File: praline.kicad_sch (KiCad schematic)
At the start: 0 parts

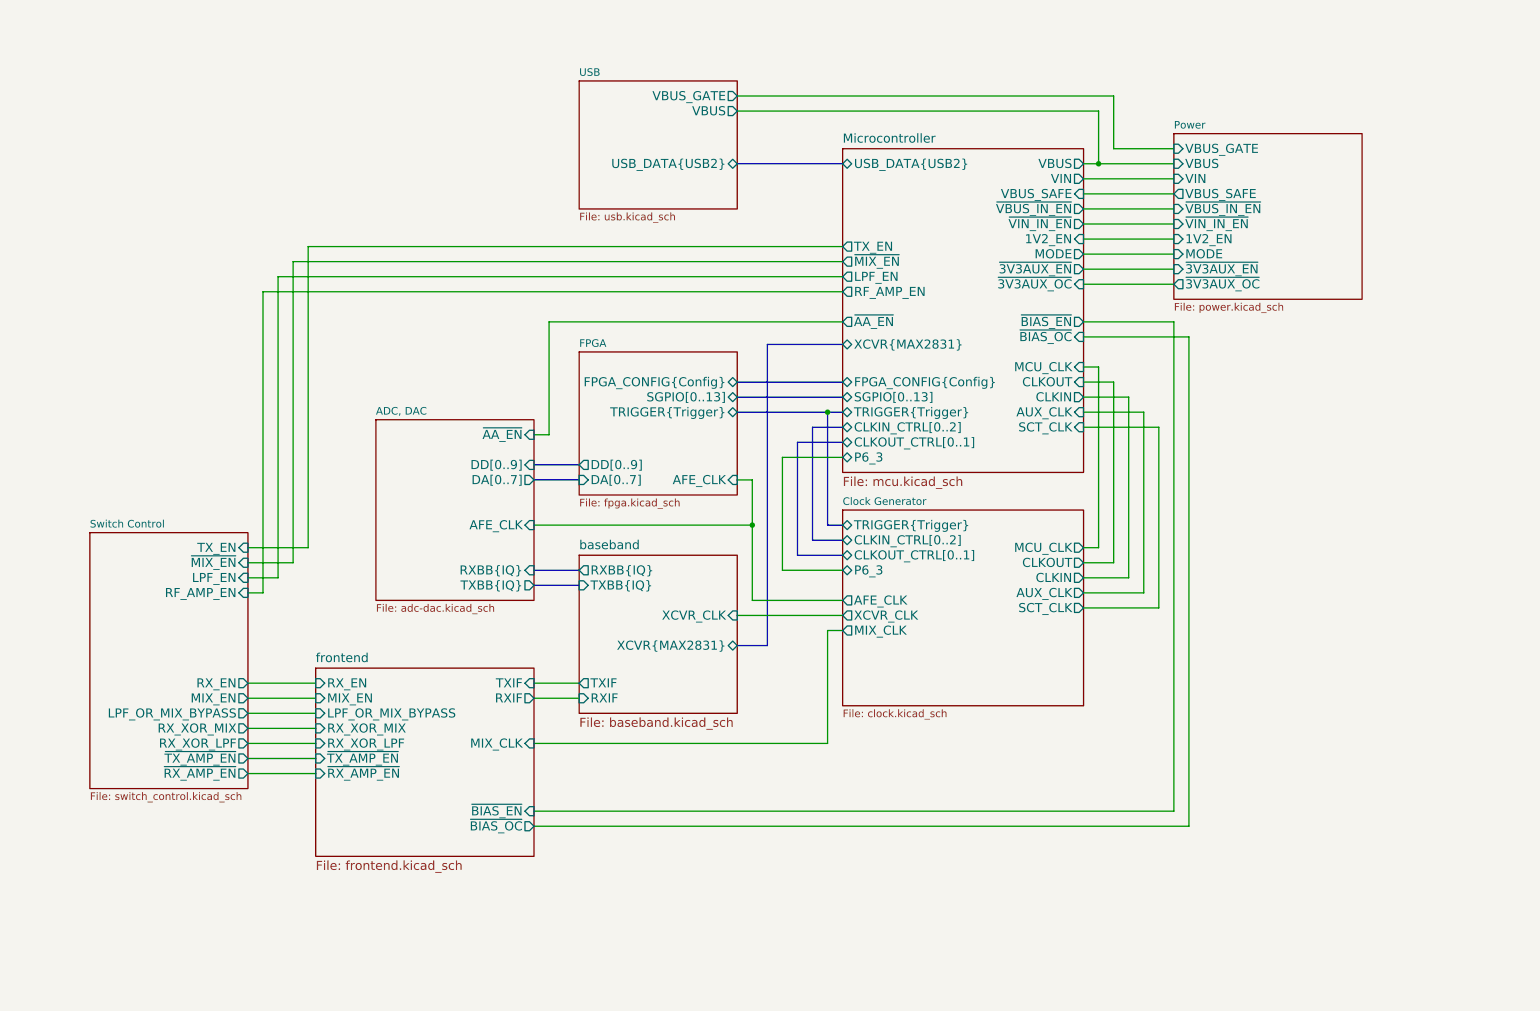
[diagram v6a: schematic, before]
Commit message: Connect mixer U4 LD and ENBL pins to MCU
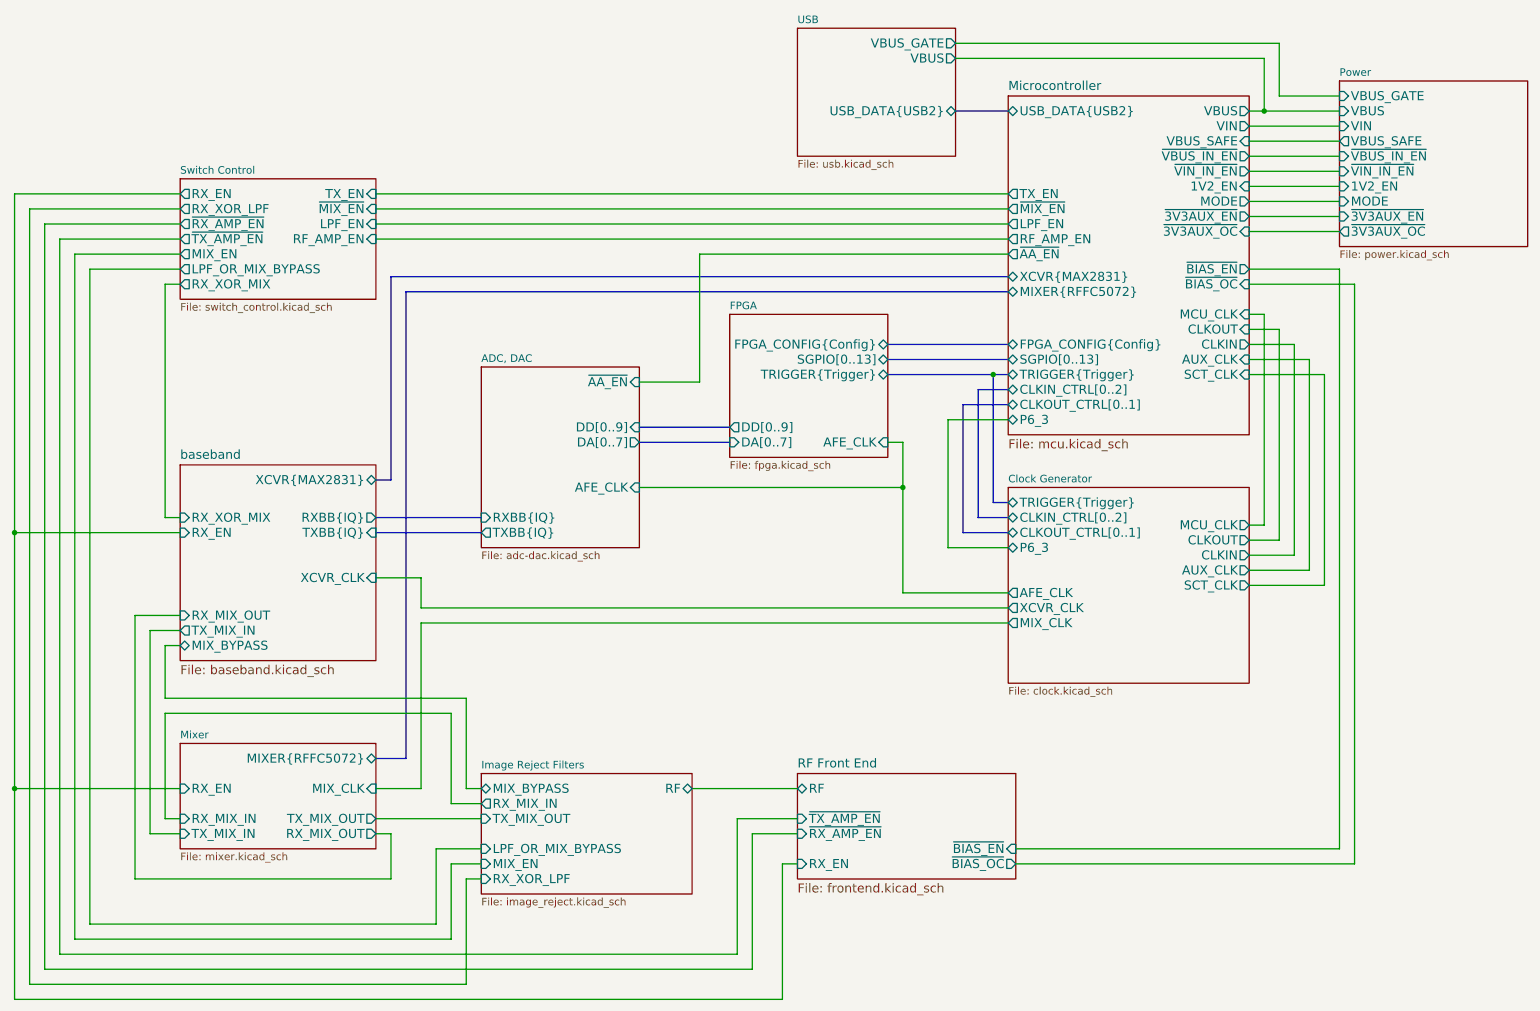
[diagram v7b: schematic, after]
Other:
- sheet frontend renamed RF Front End
- added sheet Image Reject Filters (image_reject.kicad_sch)
- added sheet Mixer (mixer.kicad_sch)
- sheet Microcontroller ports: added MIXER{RFFC5072}; removed none
- sheet RF Front End ports: added RF; removed LPF_OR_MIX_BYPASS, MIX_CLK, MIX_EN, RXIF, RX_XOR_LPF, RX_XOR_MIX, TXIF
- sheet baseband ports: added MIX_BYPASS, RX_EN, RX_MIX_OUT, RX_XOR_MIX, TX_MIX_IN; removed RXIF, TXIF

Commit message: Remove GND zone from front layer F.Cu
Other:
- sheet baseband renamed IF Transceiver
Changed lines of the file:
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@@
 			)
 		)
-		(pin "1V2_EN" input
+		(pin "1V2_EN" output
 			(at 233.68 43.18 0)
 			(effects
@@
 			)
 		)
-		(pin "VBUS" output
+		(pin "VBUS" input
 			(at 233.68 30.48 0)
 			(effects
@@
 			(color 0 0 0 0.0000)
 		)
-		(property "Sheetname" "baseband"
+		(property "Sheetname" "IF Transceiver"
 			(at 53.34 89.3314 0)
 			(effects
@@
 			)
 		)
-		(pin "CLKIN" output
+		(pin "CLKIN" input
 			(at 233.68 105.41 0)
 			(effects
